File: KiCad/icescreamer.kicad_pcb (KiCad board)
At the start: 2 copper layers, 60 x 20 mm, 84 parts, among them J1 Audio-Jack-3_3Switches, J2 Audio-Jack-3_3Switches, Q1 2SC1815, Q2 2SC1815, Q20 2SC1815, Q21 2SC1815, Q22 2SC1815, Q23 Q_NJFET_SGD, Q24 Q_NJFET_SGD, SW1 SW_TPDT, SW20 SW_Push, U1 NE5532

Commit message: Colocando componentes
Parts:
- Q23, Q24: moved to B.Cu
- moved R13 146.7 mm to (65.6, 107.5), turned to 180 degrees
- moved C13 144.5 mm to (68.7, 113.0), turned to 180 degrees
- moved R18 143.9 mm to (65.6, 102.0), turned to 180 degrees
- moved R14 133.6 mm to (70.8, 101.5), turned to 180 degrees
- moved C12 126.9 mm to (75.8, 106.9), turned to 180 degrees
- moved J1 120.3 mm to (228.0, 109.5), turned to 180 degrees
- moved R9 111.5 mm to (80.4, 92.5), turned to 180 degrees
- moved POT3 99.5 mm to (232.5, 67.5)
- moved POT1 99.4 mm to (194.5, 67.5)
- moved J2 98.9 mm to (199.0, 109.5)
- moved U1 96.1 mm to (213.5, 92.0), turned to 90 degrees
- moved BT1 94.1 mm to (241.5, 138.0), turned to 270 degrees
- moved C3 93.4 mm to (241.5, 131.0), turned to 180 degrees
- moved C6 93.4 mm to (204.0, 94.5), turned to 180 degrees
- moved R33 91.3 mm to (130.5, 139.5), turned to 180 degrees
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
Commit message: Colocando componentes II
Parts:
- moved R9 134.8 mm to (213.0, 68.0)
- moved R10 122.3 mm to (213.0, 63.5)
- moved C8 37.5 mm to (190.0, 85.0)
- moved R8 36.6 mm to (198.0, 91.5)
- moved D2 11.0 mm to (187.0, 88.5)
- moved D3 11.0 mm to (193.0, 88.5)
- moved R7 6.71 mm to (204.0, 88.5)
- moved Q1 3.35 mm to (190.5, 92.0), turned to 270 degrees
- moved U1 2.00 mm to (213.5, 94.0)
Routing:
- net PSEUDO_IN_1: track 0.00 -> 15.2 mm
- net Net-(C6-Pad1): track 0.00 -> 14.5 mm
- net Net-(Q1-Pad3): track 0.00 -> 14.2 mm
- net Net-(C5-Pad1): track 0.00 -> 2.84 mm
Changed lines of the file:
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@@
   (general
     (links 171)
-    (no_connects 165)
+    (no_connects 157)
     (area 94.335559 56.794441 286.333334 172.075001)
     (thickness 1.6)
     (drawings 19)
-    (tracks 0)
+    (tracks 27)
     (zones 0)
     (modules 84)
@@
   )
   (module drawdio:Resistor_SMD+THT (layer F.Cu)
-    (at 152.5 84 180)
+    (at 190 85 180)
     (descr "Resistor, SMD and THT, universal, 0805 to 1206,RM10,  Hand soldering,")
     (tags "Resistor, SMD and THT, universal, 0805 to 1206, RM10, Hand soldering,")
@@
   )
   (module Diodes_SMD:D_SOD-323_HandSoldering (layer F.Cu)
-    (at 198 88.5 180)
+    (at 187 88.5 180)
     (descr SOD-323)
     (tags SOD-323)
@@
   )
   (module Diodes_SMD:D_SOD-323_HandSoldering (layer F.Cu)
-    (at 204 88.5 180)
+    (at 193 88.5 180)
     (descr SOD-323)
     (tags SOD-323)
@@
   )
   (module drawdio:TO-92_SOT23_JorFru_compact (layer F.Cu)
-    (at 187.5 93.5)
+    (at 190.5 92 270)
     (descr "TO-92 leads molded, narrow, oval pads, drill 0.8mm (see NXP sot054_po.pdf)")
     (tags "to-92 sc-43 sc-43a sot54 PA33 transistor")
-    (fp_text reference Q1 (at 0 -4) (layer F.SilkS)
+    (fp_text reference Q1 (at 0 -4 270) (layer F.SilkS)
       (effects (font (size 1 1) (thickness 0.15)))
     )
-    (fp_text value 2SC1815 (at 0 3 180) (layer F.Fab)
+    (fp_text value 2SC1815 (at 0 3 450) (layer F.Fab)
       (effects (font (size 1 1) (thickness 0.15)))
     )
@@
     (fp_line (start -1.4 -2.65) (end 3.95 -2.65) (layer F.CrtYd) (width 0.05))
     (fp_line (start 3.95 1.95) (end 3.95 -2.65) (layer F.CrtYd) (width 0.05))
-    (pad 2 smd rect (at 1.26 -0.91) (size 0.8 1.1) (layers F.Cu F.Paste F.Mask)
+    (pad 2 smd rect (at 1.26 -0.91 270) (size 0.8 1.1) (layers F.Cu F.Paste F.Mask)
       (net 1 LED_ANODE))
-    (pad 1 smd rect (at 0.25 1.07) (size 0.8 1.1) (layers F.Cu F.Paste F.Mask)
+    (pad 1 smd rect (at 0.25 1.07 270) (size 0.8 1.1) (layers F.Cu F.Paste F.Mask)
       (net 8 PSEUDO_IN_1))
-    (pad 2 thru_hole oval (at 1.27 -1.905 90) (size 2.3 1.524) (drill 0.762) (layers *.Cu *.Mask F.SilkS)
+    (pad 2 thru_hole oval (at 1.27 -1.905) (size 2.3 1.524) (drill 0.762) (layers *.Cu *.Mask F.SilkS)
       (net 1 LED_ANODE))
-    (pad 1 thru_hole oval (at -0.5 0.5) (size 2.3 1.524) (drill 0.762) (layers *.Cu *.Mask F.SilkS)
+    (pad 1 thru_hole oval (at -0.5 0.5 270) (size 2.3 1.524) (drill 0.762) (layers *.Cu *.Mask F.SilkS)
       (net 8 PSEUDO_IN_1))
-    (pad 3 thru_hole oval (at 3 0.5) (size 2.3 1.524) (drill 0.762) (layers *.Cu *.Mask F.SilkS)
+    (pad 3 thru_hole oval (at 3 0.5 270) (size 2.3 1.524) (drill 0.762) (layers *.Cu *.Mask F.SilkS)
       (net 48 "Net-(Q1-Pad3)"))
-    (pad 3 smd rect (at 2.25 1.07) (size 0.8 1.1) (layers F.Cu F.Paste F.Mask)
+    (pad 3 smd rect (at 2.25 1.07 270) (size 0.8 1.1) (layers F.Cu F.Paste F.Mask)
       (net 48 "Net-(Q1-Pad3)"))
     (model Housings_TO-92.3dshapes/TO-92_Molded_Narrow_Oval.wrl
@@
   )
   (module Resistors_SMD:R_0805_HandSoldering (layer F.Cu)
-    (at 198 91.5)
+    (at 204 88.5)
     (descr "Resistor SMD 0805, hand soldering")
     (tags "resistor 0805")
@@
   )
   (module Resistors_SMD:R_0805_HandSoldering (layer F.Cu)
-    (at 168 112.5 180)
+    (at 198 91.5 180)
     (descr "Resistor SMD 0805, hand soldering")
     (tags "resistor 0805")
@@
   )
   (module Resistors_SMD:R_0805_HandSoldering (layer F.Cu)
-    (at 80.43944 92.450559 180)
+    (at 213 68 180)
     (descr "Resistor SMD 0805, hand soldering")
     (tags "resistor 0805")
@@
   )
   (module Resistors_SMD:R_0805_HandSoldering (layer F.Cu)
-    (at 91.92944 80.840559 180)
+    (at 213 63.5 180)
     (descr "Resistor SMD 0805, hand soldering")
     (tags "resistor 0805")
@@
   )
   (module footprints:DIP8+SOIC8_2 (layer F.Cu)
-    (at 213.5 92 90)
+    (at 213.5 94 90)
     (descr "8-Lead Plastic Small Outline (SN) - Narrow, 3.90 mm Body [SOIC] (see Microchip Packaging Specification 00000049BS.pdf)")
     (tags "SOIC 1.27")
@@
   (gr_arc (start 191.46 55.98) (end 190.46 55.98) (angle 90) (layer Eco2.User) (width 0.2))
   (gr_arc (start 184.46 55.98) (end 190.46 55.98) (angle 90) (layer Eco2.User) (width 0.2))
+  (segment (start 202.75 91.5) (end 202.65 91.5) (width 0.25) (layer F.Cu) (net 4))
+  (segment (start 193.81 97.5) (end 196.65 97.5) (width 0.25) (layer F.Cu) (net 5))
+  (segment (start 205.25 94.5) (end 207.02 92.73) (width 0.25) (layer F.Cu) (net 7) (status 400000))
+  (segment (start 207.02 92.73) (end 210.23 92.73) (width 0.25) (layer F.Cu) (net 7) (status 800000))
+  (segment (start 210.23 92.73) (end 211.23 92.73) (width 0.25) (layer F.Cu) (net 7) (status 400000))
+  (segment (start 213 94.5) (end 213 96.565) (width 0.25) (layer F.Cu) (net 7) (status 800000))
+  (segment (start 211.23 92.73) (end 213 94.5) (width 0.25) (layer F.Cu) (net 7))
+  (segment (start 213 96.565) (end 212.865 96.7) (width 0.25) (layer F.Cu) (net 7) (status C00000))
+  (segment (start 205.25 94.5) (end 205.25 91.6) (width 0.25) (layer F.Cu) (net 7))
+  (segment (start 205.25 91.6) (end 205.35 91.5) (width 0.25) (layer F.Cu) (net 7))
+  (segment (start 190 91.5) (end 193.5 91.5) (width 0.25) (layer F.Cu) (net 8))
+  (segment (start 193.65 91.5) (end 196.65 94.5) (width 0.25) (layer F.Cu) (net 8))
+  (segment (start 193.5 91.5) (end 193.65 91.5) (width 0.25) (layer F.Cu) (net 8))
+  (segment (start 196.65 94.5) (end 197 94.5) (width 0.25) (layer F.Cu) (net 8))
+  (segment (start 197 94.5) (end 198.5 96) (width 0.25) (layer F.Cu) (net 8))
+  (segment (start 198.5 96) (end 201.25 96) (width 0.25) (layer F.Cu) (net 8))
+  (segment (start 201.25 96) (end 202.75 94.5) (width 0.25) (layer F.Cu) (net 8))
+  (segment (start 190 95) (end 190.5 95.5) (width 0.25) (layer F.Cu) (net 48))
+  (segment (start 190.5 95.5) (end 195 95.5) (width 0.25) (layer F.Cu) (net 48))
+  (segment (start 195 95.5) (end 195.5 96) (width 0.25) (layer F.Cu) (net 48))
+  (segment (start 195.5 96) (end 197.5 96) (width 0.25) (layer F.Cu) (net 48))
+  (segment (start 197.5 96) (end 198.5 97) (width 0.25) (layer F.Cu) (net 48))
+  (segment (start 198.5 97) (end 198.85 97) (width 0.25) (layer F.Cu) (net 48))
+  (segment (start 198.85 97) (end 199.35 97.5) (width 0.25) (layer F.Cu) (net 48))
+  (segment (start 199.35 97.5) (end 199 97.5) (width 0.25) (layer F.Cu) (net 48))
+  (segment (start 199.35 97.5) (end 199.35 97.35) (width 0.25) (layer F.Cu) (net 48))
+  (segment (start 199.35 97.5) (end 202.65 97.5) (width 0.25) (layer F.Cu) (net 48))
 )

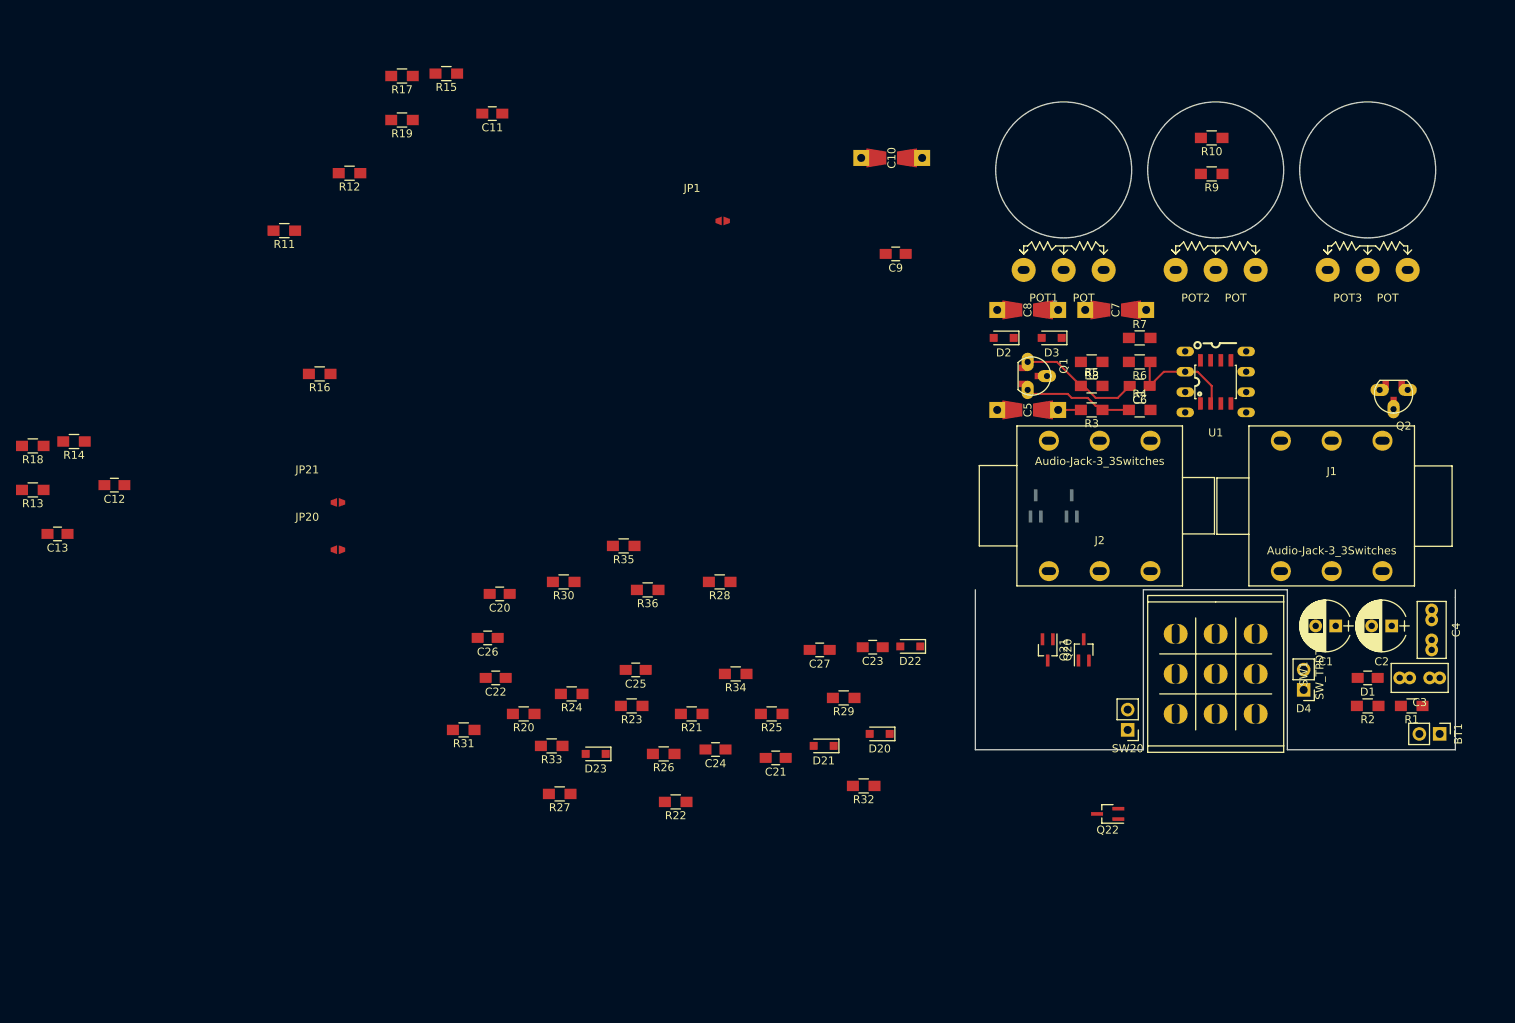
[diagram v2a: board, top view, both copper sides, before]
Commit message: pseudo circuit laid out
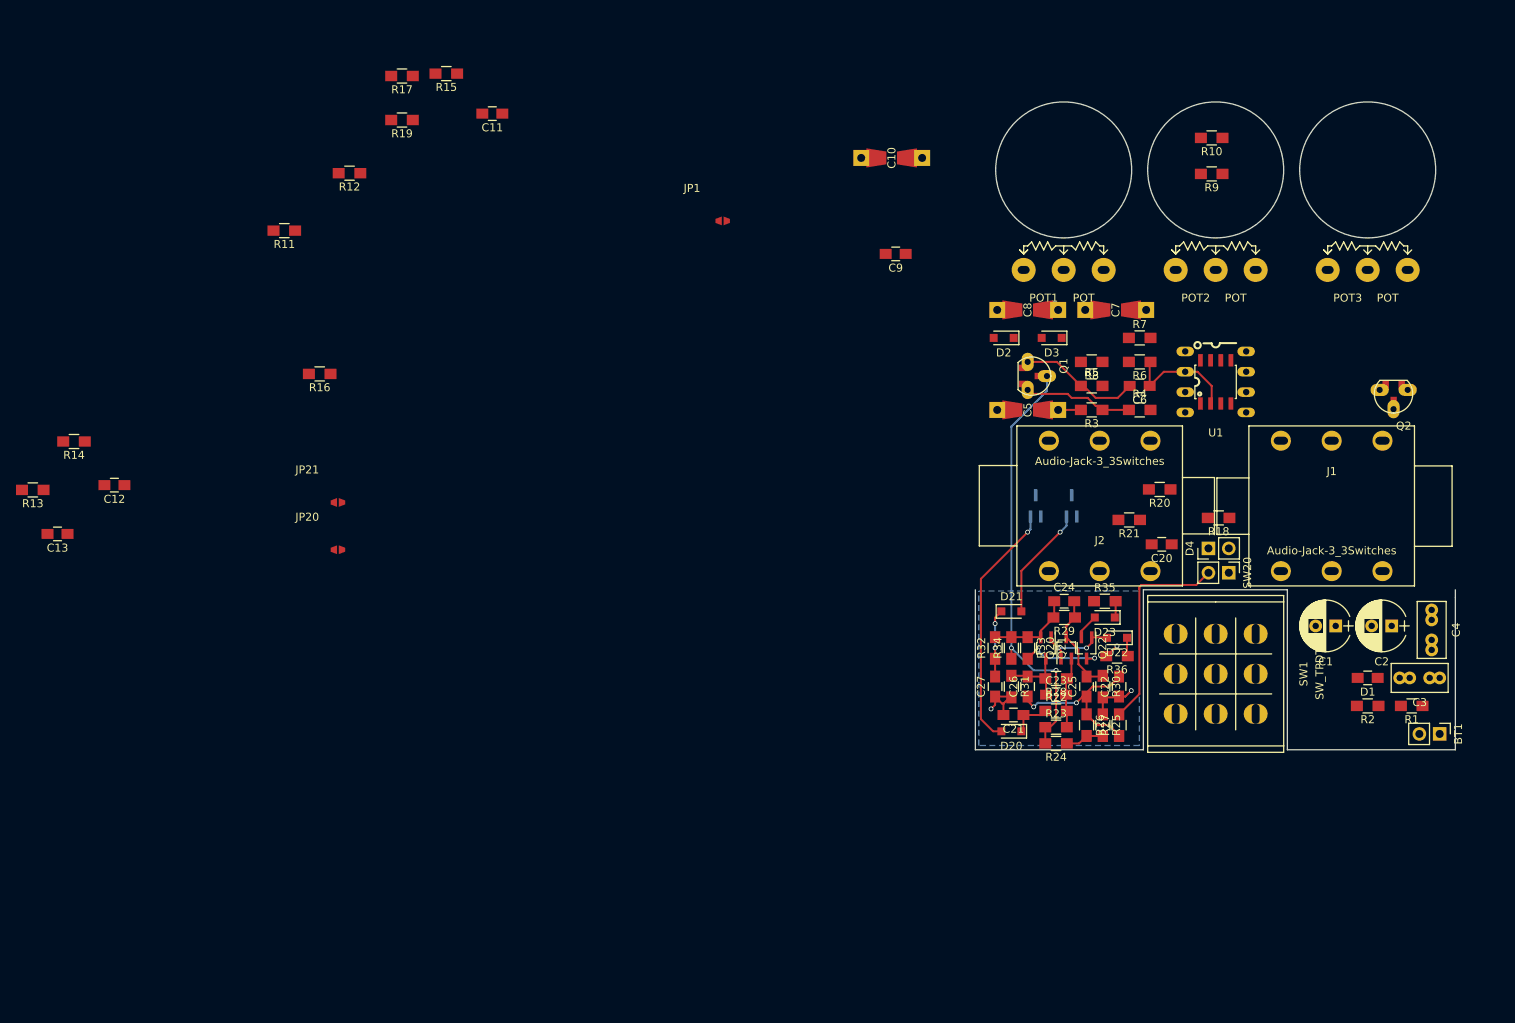
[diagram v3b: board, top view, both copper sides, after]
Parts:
- moved R18 148.5 mm to (213.9, 111.0)
- moved R20 84.3 mm to (206.5, 107.4)
- moved C20 83.0 mm to (206.8, 114.3)
- moved C22 77.9 mm to (201.4, 132.1), turned to 90 degrees
- moved R27 70.4 mm to (201.4, 136.9), turned to 90 degrees
- moved R31 68.7 mm to (188.0, 132.1), turned to 270 degrees
- moved R30 68.6 mm to (199.4, 132.1), turned to 270 degrees
- moved C26 67.8 mm to (190.0, 132.1), turned to 90 degrees
- moved D23 65.9 mm to (199.6, 123.4)
- moved R24 60.9 mm to (193.5, 139.2)
- moved R33 60.7 mm to (190.0, 127.3), turned to 270 degrees
- moved R35 60.5 mm to (199.6, 121.4), turned to 0 degrees
- moved R21 59.8 mm to (202.7, 111.3)
- moved R36 59.2 mm to (201.2, 128.3)
- moved C25 56.4 mm to (197.4, 132.1), turned to 90 degrees
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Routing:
- net LED_ANODE: track 0.00 -> 55.1 mm, vias 0 -> 2
- net Net-(D20-Pad2): track 0.00 -> 31.1 mm, vias 0 -> 1
- net Net-(R27-Pad2): track 0.00 -> 26.3 mm
- net Net-(C22-Pad2): track 0.00 -> 21.6 mm, vias 0 -> 2
- net -VDC: track 0.00 -> 15.7 mm, vias 0 -> 3
- net Net-(D21-Pad2): track 0.00 -> 14.2 mm, vias 0 -> 1
- net Net-(C24-Pad2): track 0.00 -> 13.0 mm
- net Net-(D22-Pad2): track 0.00 -> 11.7 mm, vias 0 -> 2
- net Net-(C24-Pad1): track 0.00 -> 10.8 mm
- net Net-(Q22-Pad3): track 0.00 -> 10.3 mm, vias 0 -> 2
- net Net-(C23-Pad1): track 0.00 -> 9.27 mm
- net Net-(C23-Pad2): track 0.00 -> 8.89 mm
- net Net-(C27-Pad2): track 0.00 -> 8.47 mm, vias 0 -> 2
- net Net-(C21-Pad1): track 0.00 -> 5.67 mm
- net Net-(R24-Pad1): track 0.00 -> 4.88 mm
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- added copper zone on B.Cu, net -VDC

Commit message: JorFru approved
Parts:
- added J3: Barrel_Jack_Switch, Connector_PinHeader_2.54mm:PinHeader_1x03_P2.54mm_Vertical, F.Cu at (240.8, 125.6)
- BT1, SW20: footprint Socket_Strips:Socket_Strip_Straight_1x02_Pitch2.54mm -> drawdio:1x02_P2.54mm_Hole
- C1, C2: footprint Capacitors_THT:CP_Radial_D6.3mm_P2.50mm -> Capacitor_THT:CP_Radial_D6.3mm_P2.50mm
- C10, C7, C8: footprint drawdio:Resistor_SMD+THT -> Capacitor_THT:C_Rect_L7.0mm_W3.5mm_P2.50mm_P5.00mm
- C11, C12, C13, C20, C21, C22, C23, C24, C25, C26, C27, C6, C9: footprint Capacitors_SMD:C_0805_HandSoldering -> Capacitor_SMD:C_0805_2012Metric_Pad1.15x1.40mm_HandSolder
- C3, C4: footprint Capacitors_THT:C_Rect_L7.0mm_W3.5mm_P2.50mm_P5.00mm -> Capacitor_SMD:C_0805_2012Metric_Pad1.15x1.40mm_HandSolder
- C5: footprint drawdio:Resistor_SMD+THT -> Capacitor_SMD:C_0805_2012Metric_Pad1.15x1.40mm_HandSolder
- D1: footprint Capacitors_SMD:C_0805_HandSoldering -> Diode_THT:D_DO-41_SOD81_P7.62mm_Horizontal
- D2, D3: footprint Diodes_SMD:D_SOD-323_HandSoldering -> Diode_SMD:D_MELF-RM10_Universal_Handsoldering
- D20, D21, D22: footprint Diodes_SMD:D_SOD-323_HandSoldering -> Diode_SMD:D_0805_2012Metric_Pad1.15x1.40mm_HandSolder
- D23: footprint Diodes_SMD:D_SOD-323_HandSoldering -> Diode_SMD:D_MiniMELF_Handsoldering
- D4: footprint Pin_Headers:Pin_Header_Straight_1x02_Pitch2.54mm -> Connector_PinHeader_2.54mm:PinHeader_1x02_P2.54mm_Vertical
- JP1, JP20, JP21: footprint def-footprints:Miscellaneous_Solder_Jumper -> Jumper:SolderJumper-2_P1.3mm_Open_RoundedPad1.0x1.5mm
- POT1, POT2, POT3: footprint footprints:IcePOT -> Connector_PinHeader_2.54mm:PinHeader_1x03_P2.54mm_Vertical
- Q20, Q21, Q22: footprint TO_SOT_Packages_SMD:SOT-323_SC-70_Handsoldering -> drawdio:TO-92_SOT23_JorFru_compact
- Q23, Q24: footprint TO_SOT_Packages_SMD:SOT-323_SC-70_Handsoldering -> drawdio:TO-92_SOT23_JorFru_compact; moved to F.Cu
- R1, R10, R11, R12, R13, R14, R15, R16, R17, R18, R19, R2, R20, R21, R22, R23, R24, R25, R26, R27, R28, R29, R3, R30, R31, R32, R33, R34, R35, R36, R4, R5, R6, R7, R8, R9: footprint Resistors_SMD:R_0805_HandSoldering -> Resistor_SMD:R_0805_2012Metric_Pad1.15x1.40mm_HandSolder
- moved C13 166.4 mm to (232.2, 81.9)
- moved R14 163.6 mm to (232.2, 74.3)
- moved R13 162.0 mm to (224.2, 74.3)
- moved C12 160.2 mm to (232.2, 71.8)
- moved R16 131.4 mm to (232.2, 79.4), turned to 0 degrees
- moved R11 127.1 mm to (224.2, 76.8)
- moved R17 121.1 mm to (232.2, 69.2)
- moved R15 116.8 mm to (232.2, 76.8)
- moved R19 112.6 mm to (224.2, 69.2)
- moved JP21 109.7 mm to (213.4, 113.2)
- moved JP20 109.6 mm to (213.3, 116.2)
- moved R12 108.4 mm to (213.6, 71.8), turned to 0 degrees
- moved C11 101.7 mm to (224.2, 71.8)
- moved JP1 76.7 mm to (228.2, 65.9), turned to 0 degrees
- moved C3 63.2 mm to (213.6, 74.3)
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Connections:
- BT1 pad 1: LED_ANODE -> Net-(BT1-Pad1)
- C1 pad 1: LED_ANODE -> +VDC
- C3 pad 1: LED_ANODE -> +VDC
- D1 pad 1: LED_ANODE -> +VDC
- D4 pad 2: LED_ANODE -> +VDC
- J1 pad 5: Net-(J1-Pad5) -> (no net)
- J1 pad 6: Net-(J1-Pad6) -> (no net)
- J2 pad 4: Net-(J2-Pad4) -> (no net)
- J2 pad 5: Net-(J2-Pad5) -> (no net)
- J2 pad 6: Net-(J2-Pad6) -> (no net)
- POT1 pad 3: Net-(POT1-Pad3) -> (no net)
- Q1 pad 2: LED_ANODE -> +VDC
- Q2 pad 2: LED_ANODE -> +VDC
- R1 pad 1: LED_ANODE -> +VDC
- R23 pad 1: LED_ANODE -> +VDC
- R24 pad 2: LED_ANODE -> +VDC
- R34 pad 1: LED_ANODE -> +VDC
- SW1 pad 32: Net-(SW1-Pad32) -> (no net)
- U1 pad 2: Net-(C6-Pad1) -> Net-(C7-Pad2)
- U1 pad 3: Net-(C7-Pad2) -> Net-(C6-Pad1)
- U1 pad 8: LED_ANODE -> +VDC
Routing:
- net GNDREF: track 0.10 -> 252.1 mm, vias 0 -> 12
- net +VDC: track 0.00 -> 212.5 mm, vias 0 -> 12
- net EFF_OUT: track 0.00 -> 94.8 mm
- net EFF_IN: track 0.00 -> 73.2 mm
- net Net-(D22-Pad2): track 11.7 -> 73.9 mm, vias 2 -> 0
- net PSEUDO_OUT: track 0.00 -> 57.3 mm, vias 0 -> 3
- net Net-(Q22-Pad3): track 10.3 -> 66.8 mm
- net LED_ANODE: track 55.1 -> 0.00 mm, vias 2 -> 0
- net Net-(C7-Pad1): track 0.00 -> 53.2 mm, vias 0 -> 2
- net Net-(D21-Pad2): track 14.2 -> 64.1 mm, vias 1 -> 2
- net Net-(C9-Pad2): track 0.00 -> 45.9 mm, vias 0 -> 1
- net Net-(C7-Pad2): track 0.00 -> 42.2 mm, vias 0 -> 1
- net Net-(POT2-Pad1): track 0.00 -> 40.2 mm
- net PSEUDO_IN_2: track 0.00 -> 35.5 mm
- net JACK_IN: track 0.00 -> 35.0 mm
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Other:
- board size 60 x 20 mm -> 60 x 85 mm
